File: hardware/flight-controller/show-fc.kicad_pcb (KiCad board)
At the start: 2 copper layers, 50 x 50 mm, 116 parts, among them J1 USB-C, J2 microSD, J3 ESC, J4 GPS, J5 LIGHT, J6 RC, J8 SWD, Q1 2N7002, SW1 BOOT, SW2 RESET, U1 RP2354B, U2 USBLC6-2SC6, U3 LMR51635YDDCR, U4 LP5912-3.3DRVR, U5 LP5912-1.8DRVR, U6 ICM-42688-P, U7 BMI270, U8 DPS368, Y1 12MHz

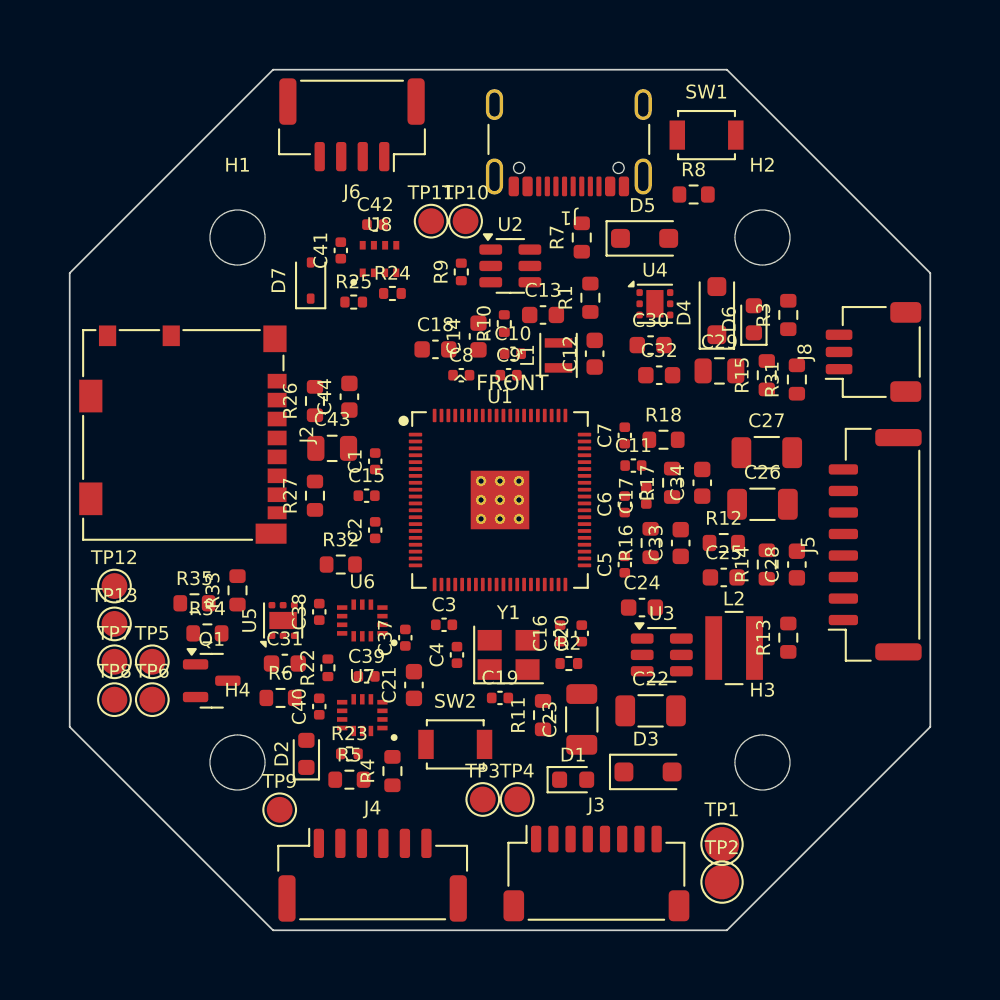
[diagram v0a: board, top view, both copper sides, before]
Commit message: Show FC: routing pipeline, 54 mm board, PCBWay rules and README (routing in progress)
Adds the Freerouting pipeline (route.py), fab export (make_fab.py), the
PCBWay .kicad_dru and the README. Widens the flats to 54 mm (corners
still 27 mm), remaps LED data to GPIO42, moves the AUX and TELEM2 pads
next to their pins and drops SD card detect.

Co-Authored-By: Claude Opus 5.5 (1M context) <noreply@anthropic.com>
Claude-Session: https://claude.ai/code/session_01BR3A1ZEFbsPLQy3Mn5HNY3
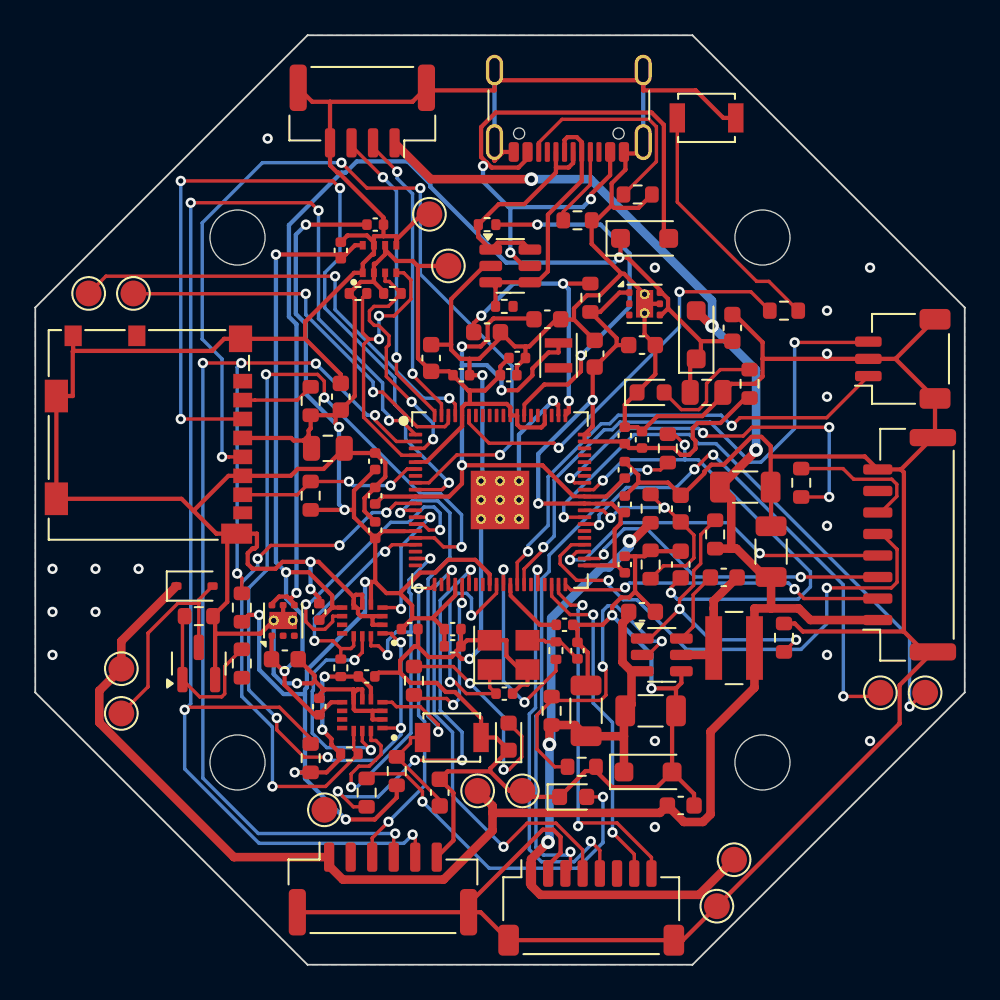
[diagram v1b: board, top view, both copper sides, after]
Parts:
- TP1, TP2: footprint TestPoint:TestPoint_Pad_D2.0mm -> TestPoint:TestPoint_Pad_D1.5mm
- U4, U5: footprint Package_SON:WSON-6-1EP_2x2mm_P0.65mm_EP1x1.6mm -> Package_SON:WSON-6-1EP_2x2mm_P0.65mm_EP1x1.6mm_ThermalVias
- moved TP8 47.1 mm to (124.7, 111.2)
- moved TP7 44.5 mm to (122.1, 111.2)
- moved TP13 19.2 mm to (78.7, 88.0)
- moved D7 19.0 mm to (82.2, 105.0), turned to 0 degrees
- moved TP12 17.1 mm to (76.1, 88.0)
- moved D2 15.7 mm to (104.2, 117.2), turned to 0 degrees
- moved C28 15.5 mm to (110.5, 117.8), turned to 0 degrees
- moved R12 15.4 mm to (104.8, 115.5)
- moved R32 11.4 mm to (89.0, 115.0), turned to 90 degrees
- moved R6 7.43 mm to (92.2, 117.0), turned to 90 degrees
- moved D6 7.35 mm to (108.8, 93.8), turned to 0 degrees
- moved R13 7.35 mm to (112.5, 102.0)
- moved R5 6.86 mm to (95.0, 110.5), turned to 90 degrees
- moved C21 6.43 mm to (96.5, 117.0)
- moved R31 6.01 mm to (117.5, 99.0)
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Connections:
- J2 pad 9: SD_DET -> (no net)
- U1 pad 28: LED_DATA -> (no net)
- U1 pad 46: SD_DET -> (no net)
- U1 pad 53: (no net) -> LED_DATA
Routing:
- net GND: track 0.00 -> 462.4 mm, vias 0 -> 25
- net +3V3: track 0.00 -> 185.8 mm, vias 0 -> 11
- net +5V: track 0.00 -> 120.3 mm, vias 0 -> 3
- net I2C0_SDA: track 0.00 -> 81.5 mm, vias 0 -> 5
- net I2C0_SCL: track 0.00 -> 66.0 mm, vias 0 -> 6
- net +4V5: track 0.00 -> 61.3 mm, vias 0 -> 2
- net SPI0_MISO: track 0.00 -> 58.2 mm, vias 0 -> 7
- net SD_SCK: track 0.00 -> 53.6 mm, vias 0 -> 4
- net VBAT: track 0.00 -> 53.3 mm, vias 0 -> 3
- net SD_MOSI: track 0.00 -> 49.4 mm, vias 0 -> 4
- net +1V8_IMU: track 0.00 -> 43.9 mm, vias 0 -> 3
- net +1V1: track 0.00 -> 41.8 mm, vias 0 -> 3
- net VBUS: track 0.00 -> 38.8 mm, vias 0 -> 3
- net AUX6: track 0.00 -> 33.9 mm, vias 0 -> 2
- net SWDIO: track 0.00 -> 33.2 mm, vias 0 -> 2
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- added copper zone on B.Cu, net GND
- added copper zone on F.Cu, net GND
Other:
- board size 50 x 50 mm -> 54 x 54 mm
- rule pad_to_mask_clearance: 0.05 -> 0

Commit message: Show FC: routed 54 mm board (4 connections left), stacking holes, fab outputs
Routes the 2-layer board with Freerouting plus a second pass (finish.py);
four connections remain for KiCad's interactive router, listed in the
README. Mounting holes follow the shared stack spec (3.3 mm unplated,
30.5 mm pattern, 7.5 mm copper-free ring). Adds Gerbers, drill, CPL and
BOM in fab/ and board renders.

Co-Authored-By: Claude Opus 5.5 (1M context) <noreply@anthropic.com>
Claude-Session: https://claude.ai/code/session_01BR3A1ZEFbsPLQy3Mn5HNY3
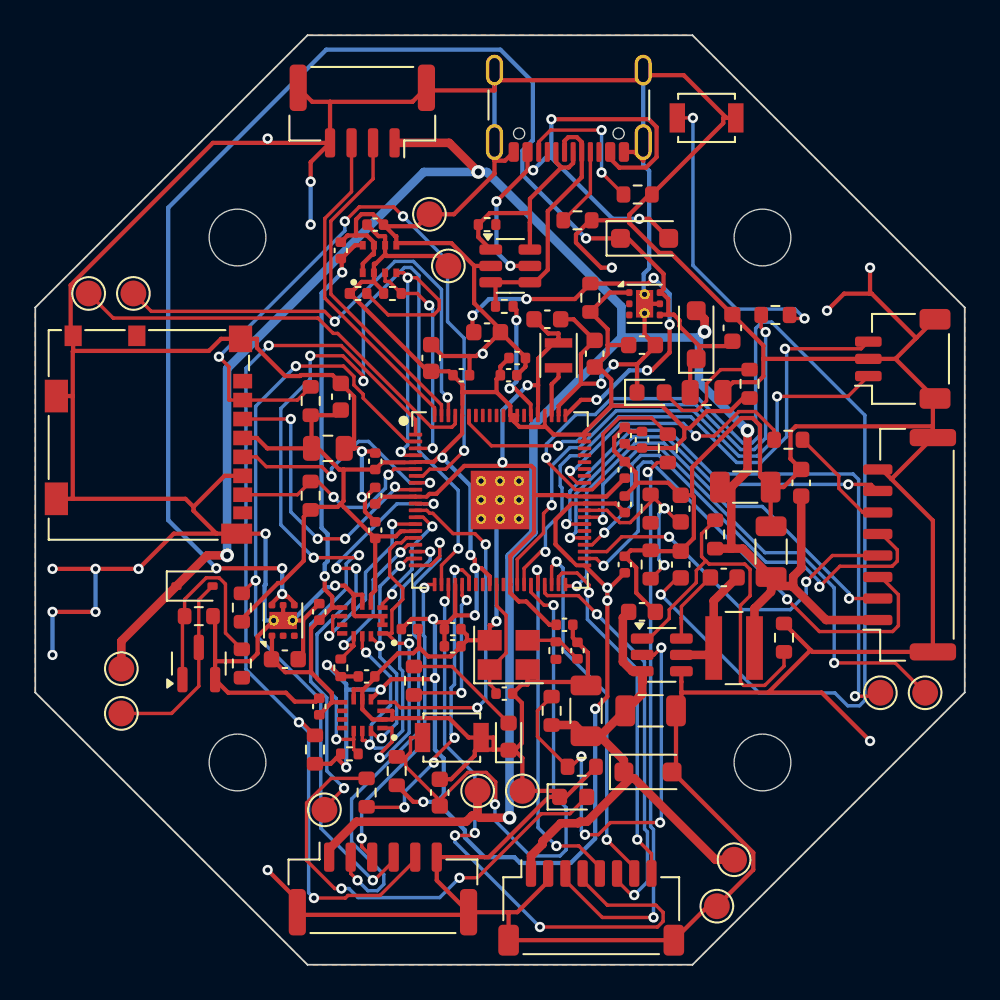
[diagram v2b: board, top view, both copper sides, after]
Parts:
- H1, H2, H3, H4: footprint MountingHole:MountingHole_3.2mm_M3 -> showfc:MountingHole_3.3mm_M3_Stack
- moved C28 20.0 mm to (117.5, 99.0), turned to 90 degrees
- moved R31 2.61 mm to (116.8, 96.5), turned to 0 degrees
- moved R3 0.56 mm to (116.0, 89.2)
- moved R32 0.56 mm to (89.2, 114.5)
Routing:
- net GPS_PPS: track 0.00 -> 65.1 mm, vias 0 -> 6
- net GND: track 462.4 -> 519.4 mm, vias 25 -> 22
- net ADC_CURR: track 29.2 -> 74.9 mm, vias 3 -> 2
- net SD_SCK: track 53.6 -> 14.3 mm, vias 4 -> 2
- net SPI0_MISO: track 58.2 -> 19.4 mm, vias 7 -> 2
- net SD_CS: track 4.27 -> 41.2 mm, vias 0 -> 4
- net SD_MOSI: track 49.4 -> 17.5 mm
- net GPS_TX: track 0.00 -> 28.8 mm, vias 0 -> 2
- net RUN: track 6.04 -> 34.3 mm, vias 0 -> 2
- net I2C0_SDA: track 81.5 -> 53.7 mm, vias 5 -> 3
- net +5V: track 120.3 -> 144.6 mm, vias 3 -> 5
- net LIGHT_IO: track 0.00 -> 23.8 mm, vias 0 -> 2
- net M2: track 0.00 -> 23.6 mm, vias 0 -> 2
- net +4V5: track 61.3 -> 82.5 mm, vias 2 -> 4
- net USB_DP: track 21.2 -> 0.00 mm, vias 2 -> 0
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
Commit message: Show FC: finish routing, add SWD debug pads, move project to KiCad 10
- Upgrade schematic, board and project to the KiCad 10 format. The schematic
  now uses global labels so its net names match the board's, and the TP
  symbol pin sits on the 1.27 mm grid; ERC is clean.
- Route the last four connections by hand:
  XOUT from U1.31 between XIN and +1V1, under Y1 to R2 (XIN narrowed to 0.15);
  USB_DP from R9 through a via inside the U2 loop, bottom layer to a via over
  U1.67 (USB_DM via and the +1V1 core link moved to make room);
  VBAT by swapping R16 and R17, so R16's VBAT pad sits beside C24;
  BUZZER from U1.27 around the mounting holes on the bottom layer to R34.
- Add five 1 mm SWD debug pads (TP14-TP18: SWDIO, GND, SWCLK, 3V3, RUN) on
  the bottom behind J8, in design.py and the schematic as test points.
- Remove two dangling stubs, set solid zone connections on four starved
  thermals. DRC with parity and zone refill: 0 errors, 0 warnings,
  0 unconnected.
- Regenerate fab outputs and renders with KiCad 10; update the README.
- handroute.py: GRID, SLACK and SIGNAL_W can be set from the environment.

Co-Authored-By: Claude Opus 5.5 (1M context) <noreply@anthropic.com>
Claude-Session: https://claude.ai/code/session_01BR3A1ZEFbsPLQy3Mn5HNY3
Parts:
- added TP14: SWDIO, TestPoint:TestPoint_Pad_D1.0mm, B.Cu at (123.6, 88.6)
- added TP15: GND, TestPoint:TestPoint_Pad_D1.0mm, B.Cu at (123.6, 91.1)
- added TP16: SWCLK, TestPoint:TestPoint_Pad_D1.0mm, B.Cu at (123.6, 93.7)
- added TP17: +3V3, TestPoint:TestPoint_Pad_D1.0mm, B.Cu at (123.6, 96.2)
- added TP18: RUN, TestPoint:TestPoint_Pad_D1.0mm, B.Cu at (123.6, 98.8)
- moved R16 3.25 mm to (108.8, 103.8)
- moved R17 3.25 mm to (108.8, 100.5)
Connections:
- J1 pad A8: (no net) -> unconnected-(J1-SBU1-PadA8)
- J1 pad B8: (no net) -> unconnected-(J1-SBU2-PadB8)
- J2 pad 1: (no net) -> unconnected-(J2-DAT2-Pad1)
- J2 pad 8: (no net) -> unconnected-(J2-DAT1-Pad8)
- J2 pad 9: (no net) -> unconnected-(J2-DET_B-Pad9)
- U1 pad 28: (no net) -> unconnected-(U1-GPIO27-Pad28)
- U1 pad 46: (no net) -> unconnected-(U1-GPIO37-Pad46)
- U1 pad 54: (no net) -> unconnected-(U1-GPIO43/ADC3-Pad54)
- U1 pad 55: (no net) -> unconnected-(U1-GPIO44/ADC4-Pad55)
- U1 pad 56: (no net) -> unconnected-(U1-GPIO45/ADC5-Pad56)
- U1 pad 57: (no net) -> unconnected-(U1-GPIO46/ADC6-Pad57)
- U1 pad 58: (no net) -> unconnected-(U1-GPIO47/ADC7-Pad58)
- U1 pad 70: (no net) -> unconnected-(U1-QSPI_SD3-Pad70)
- U1 pad 71: (no net) -> unconnected-(U1-QSPI_SCLK-Pad71)
- U1 pad 72: (no net) -> unconnected-(U1-QSPI_SD0-Pad72)
- U1 pad 73: (no net) -> unconnected-(U1-QSPI_SD2-Pad73)
- U1 pad 74: (no net) -> unconnected-(U1-QSPI_SD1-Pad74)
- U4 pad 2: (no net) -> unconnected-(U4-NC-Pad2)
- U4 pad 3: (no net) -> unconnected-(U4-PG-Pad3)
- U5 pad 2: (no net) -> unconnected-(U5-NC-Pad2)
- U5 pad 3: (no net) -> unconnected-(U5-PG-Pad3)
- U6 pad 10: (no net) -> unconnected-(U6-OCSB/RESV-Pad10)
- U6 pad 11: (no net) -> unconnected-(U6-OSDO/RESV-Pad11)
- U7 pad 10: (no net) -> unconnected-(U7-OCSB/RESV-Pad10)
- U7 pad 11: (no net) -> unconnected-(U7-OSDO/RESV-Pad11)
- U7 pad 9: (no net) -> unconnected-(U7-INT2/CLKIN-Pad9)
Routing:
- net BUZZER: track 0.00 -> 51.1 mm, vias 0 -> 4
- net RUN: track 34.3 -> 77.5 mm, vias 2 -> 5
- net USB_DP: track 0.00 -> 12.5 mm, vias 0 -> 2
- net GND: track 519.4 -> 510.5 mm, vias 22 -> 23
- net +3V3: track 190.4 -> 199.1 mm, vias 13 -> 14
- net XOUT: track 0.00 -> 6.98 mm
- net SWDIO: track 34.2 -> 37.6 mm, vias 2 -> 3
- net SWCLK: track 31.8 -> 35.0 mm, vias 2 -> 3
- net ADC_VBAT: track 12.1 -> 9.25 mm
- net VBAT: track 32.8 -> 35.2 mm
- net ADC_CURR: track 74.9 -> 74.1 mm
- net USB_DP_C: track 13.5 -> 13.0 mm
